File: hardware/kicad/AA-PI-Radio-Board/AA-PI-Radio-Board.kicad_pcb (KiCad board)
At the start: 2 copper layers, 56 x 65 mm, 79 parts, among them J1 ANT-IN, J2 MAIN BOARD, J3 INDUCT, J4 INDUCT, J5 WORK, J6 HWCAL, J7 V/I OUT, U1 Si5351A, U2 SA612A, U3 SA612A, U4 RT9193-33GB, U5 MC4558, Y1 27M

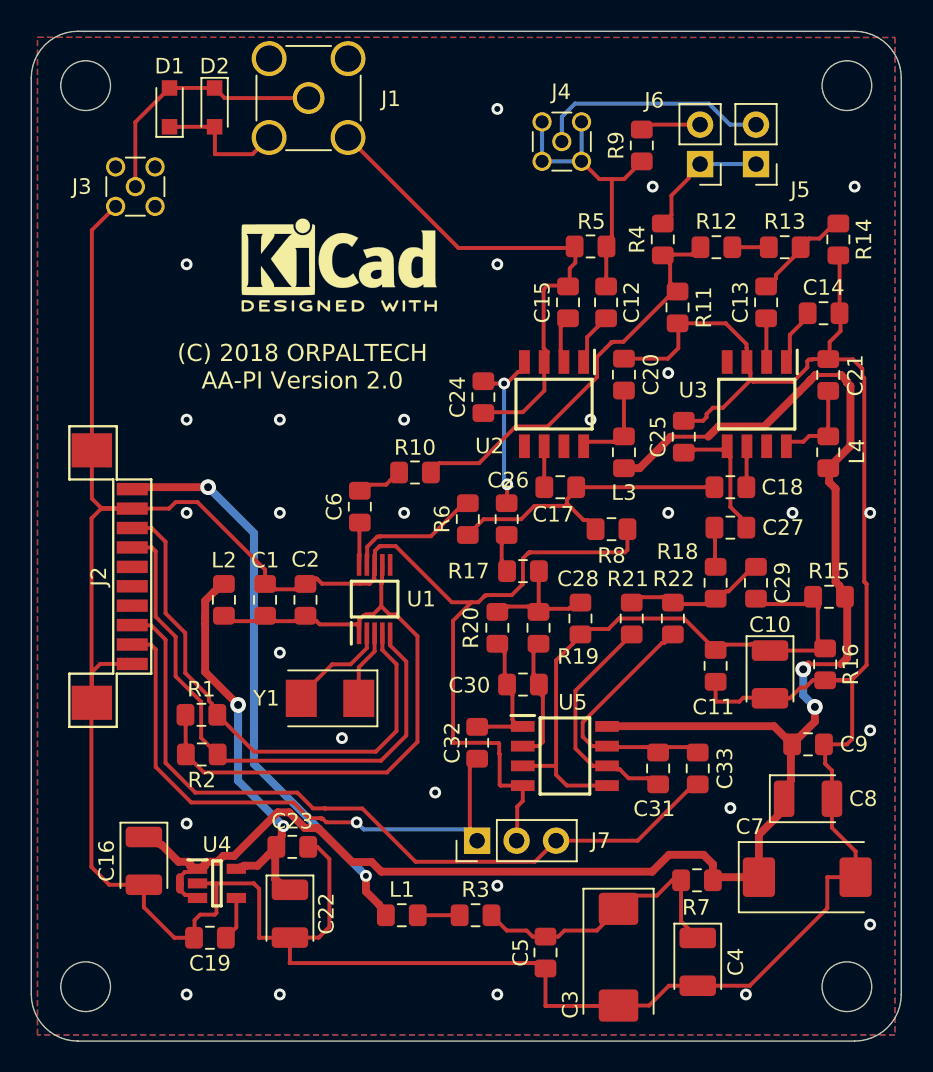
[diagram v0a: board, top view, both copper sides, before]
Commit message: Encreased thickness of the antenna route
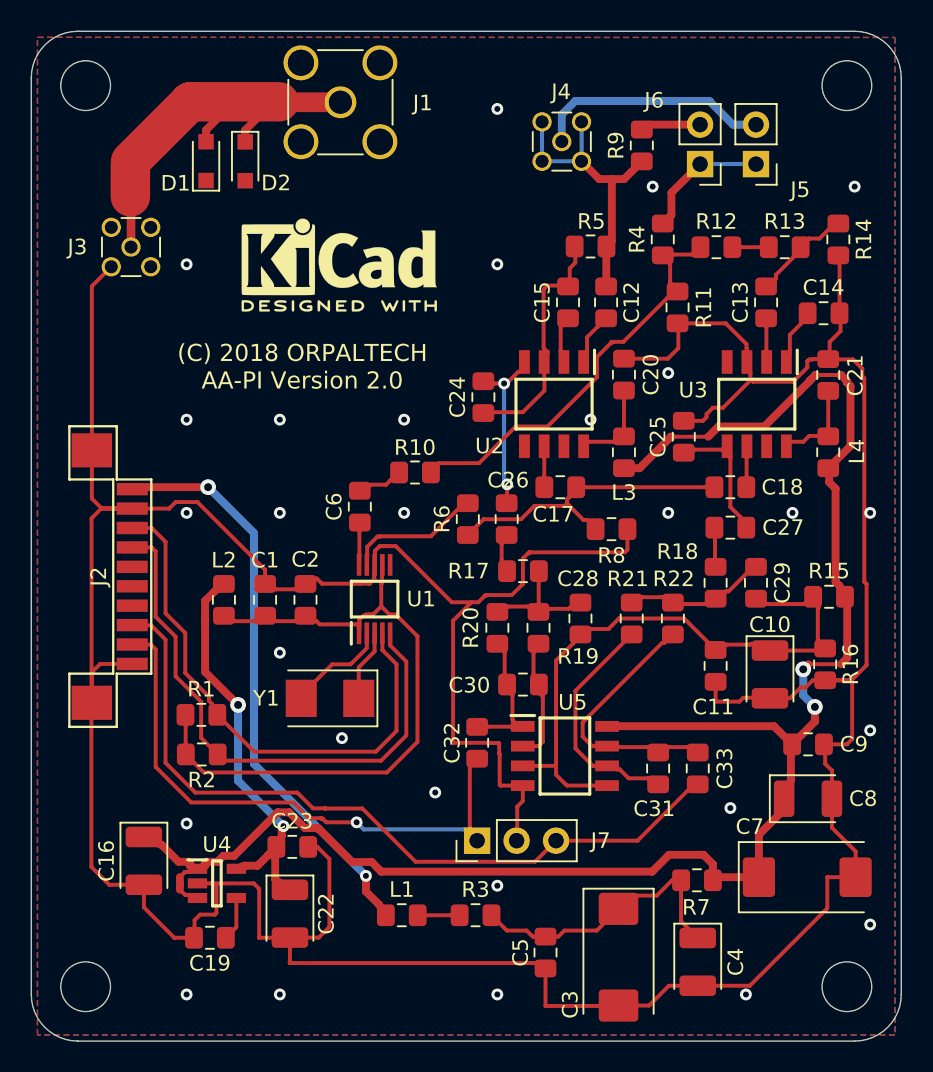
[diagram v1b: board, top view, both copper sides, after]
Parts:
- moved D1 4.18 mm to (111.2, 83.4)
- moved D2 3.99 mm to (113.8, 83.4)
- moved J3 3.90 mm to (106.4, 88.9)
- moved J1 2.07 mm to (119.9, 79.6)
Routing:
- net GND: track 321.1 -> 291.0 mm
- net Net-(D1-Pad2): track 16.6 -> 32.5 mm

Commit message: planned update (hardware)
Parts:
- removed J5: WORK, AA-PI-Footprints:PinHeader_1x02_P2.54mm_Vertical
- removed J6: HWCAL, AA-PI-Footprints:PinHeader_1x02_P2.54mm_Vertical
- removed REF**: KiCad-Logo2_6mm_SilkScreen, Symbol:KiCad-Logo2_6mm_SilkScreen
- added R23: 100K, AA-PI-Footprints:R_0805_2012Metric_Pad1.15x1.40mm_HandSolder, F.Cu at (110.5, 132.7)
- added R24: 0, AA-PI-Footprints:R_0805_2012Metric_Pad1.15x1.40mm_HandSolder, F.Cu at (107.2, 129.8)
- added SW1: HWCAL/WORK, AA-PI-Footprints:SW_SPDT_PCM12, F.Cu at (144.3, 81.7)
- C16: value 10u -> 4.7u; footprint AA-PI-Footprints:CP_EIA-3528-21_Kemet-B -> AA-PI-Footprints:C_0805_2012Metric_Pad1.15x1.40mm_HandSolder
- moved C19 1.85 mm to (113.2, 132.7), turned to 270 degrees
- moved U4 1.74 mm to (112.0, 128.1)
- moved C16 1.18 mm to (107.1, 127.2), turned to 0 degrees
- moved R9 0.87 mm to (139.0, 83.2), turned to 180 degrees
- moved C23 0.14 mm to (116.8, 127.6)
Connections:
- C16 pad 1: +5V -> GND
- C16 pad 2: GND -> +5V
- J2 pad 6: Net-(J2-Pad6) -> RADIO_EN
- U4 pad 3: +5V -> RADIO_EN
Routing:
- net RADIO_EN: track 0.00 -> 28.4 mm, vias 0 -> 2
- net GND: track 291.0 -> 299.8 mm, vias 28 -> 29
- net Net-(J4-Pad1): track 15.2 -> 10.6 mm, vias 0 -> 1
- net Net-(D1-Pad2): track 32.5 -> 34.7 mm
- net +5V: track 115.4 -> 113.4 mm
- net Net-(R4-Pad2): track 8.42 -> 10.1 mm
- net Net-(R9-Pad1): track 3.88 -> 2.82 mm
- net VI: track 19.5 -> 18.8 mm
- net +3V3: track 26.1 -> 25.4 mm
